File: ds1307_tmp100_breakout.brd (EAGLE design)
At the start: 23.5 x 23.5 mm, 11 parts

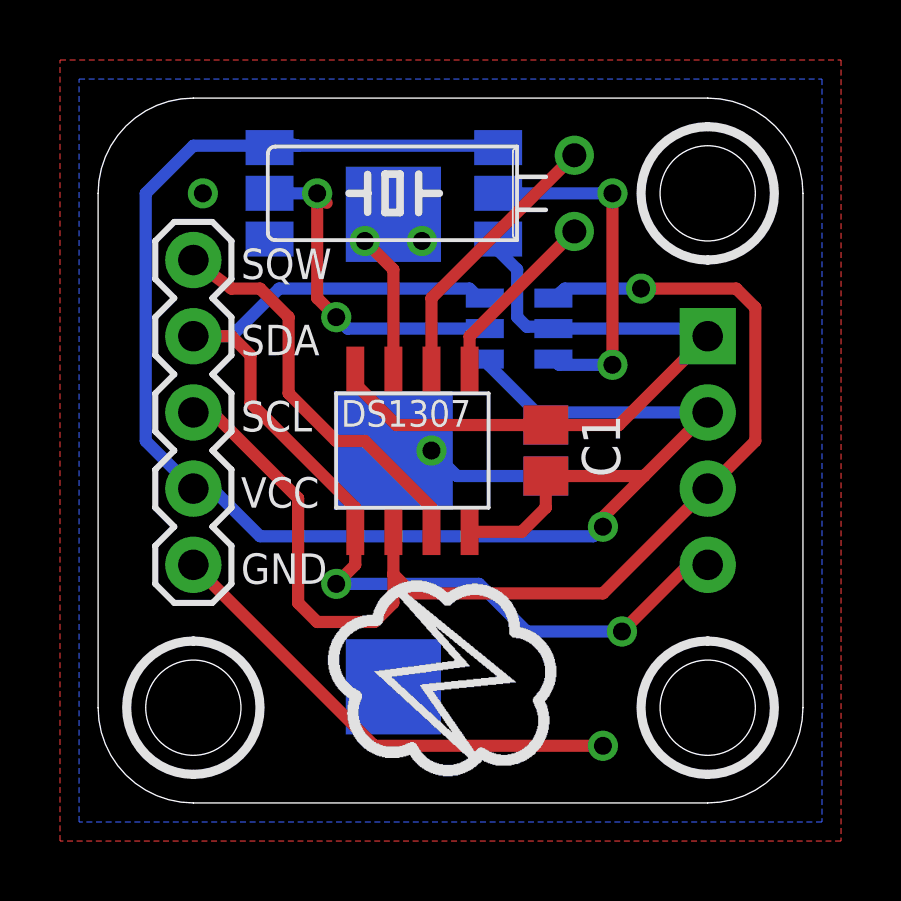
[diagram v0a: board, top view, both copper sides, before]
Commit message: reversed header on TMP100 side
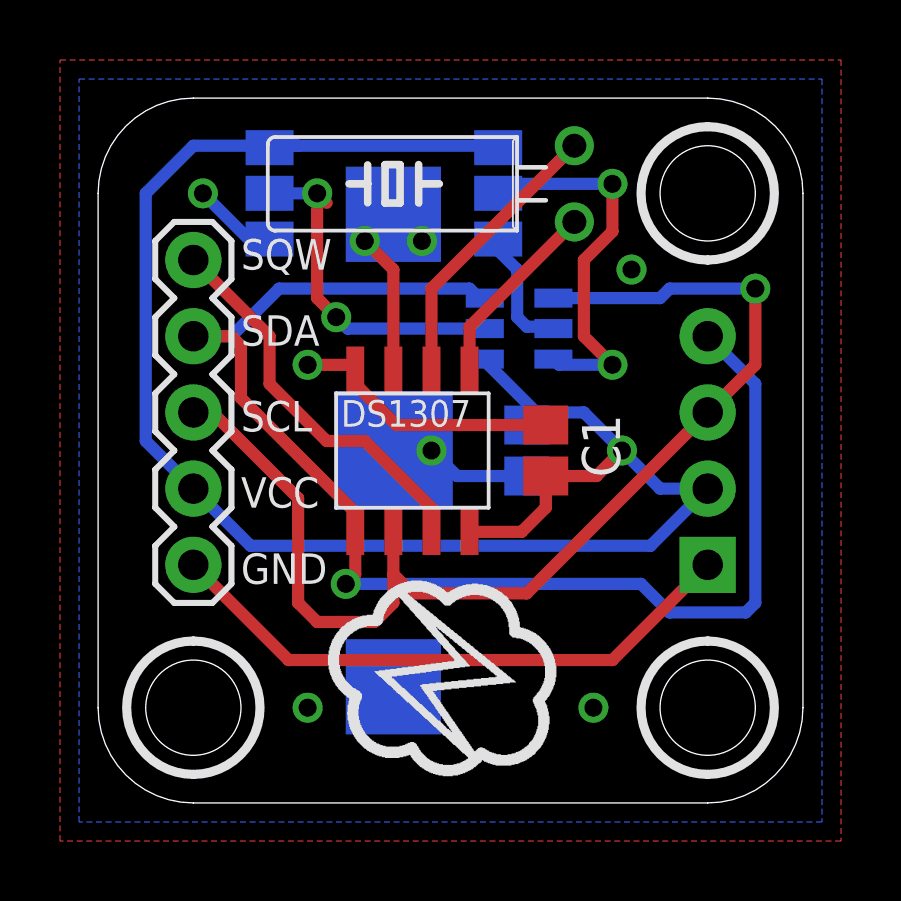
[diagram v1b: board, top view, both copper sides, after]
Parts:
- moved JP3 7.62 mm to (20.3, 7.94), turned to 90 degrees
- moved C2 0.63 mm to (14.3, 11.7)
- moved XTAL1 0.32 mm to (13.3, 20.6)
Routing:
- net SDA: track 36.0 -> 45.6 mm, vias 2 -> 1
- net GND: track 43.8 -> 39.5 mm, vias 3 -> 6
- net AD1: track 11.6 -> 12.8 mm
- net SCL: track 40.2 -> 39.1 mm
- net VCC: track 59.8 -> 60.6 mm
